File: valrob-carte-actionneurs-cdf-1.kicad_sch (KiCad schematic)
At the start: 99 parts, among them J1 USB_C_Receptacle_USB2.0_14P, J2 Conn_01x02, J3 Conn_01x02, J4 Conn_01x04_Pin, M1 Motor_Servo, M10 Motor_Servo, M11 Motor_Servo, M12 Motor_Servo, M13 Motor_Servo, M14 Motor_Servo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

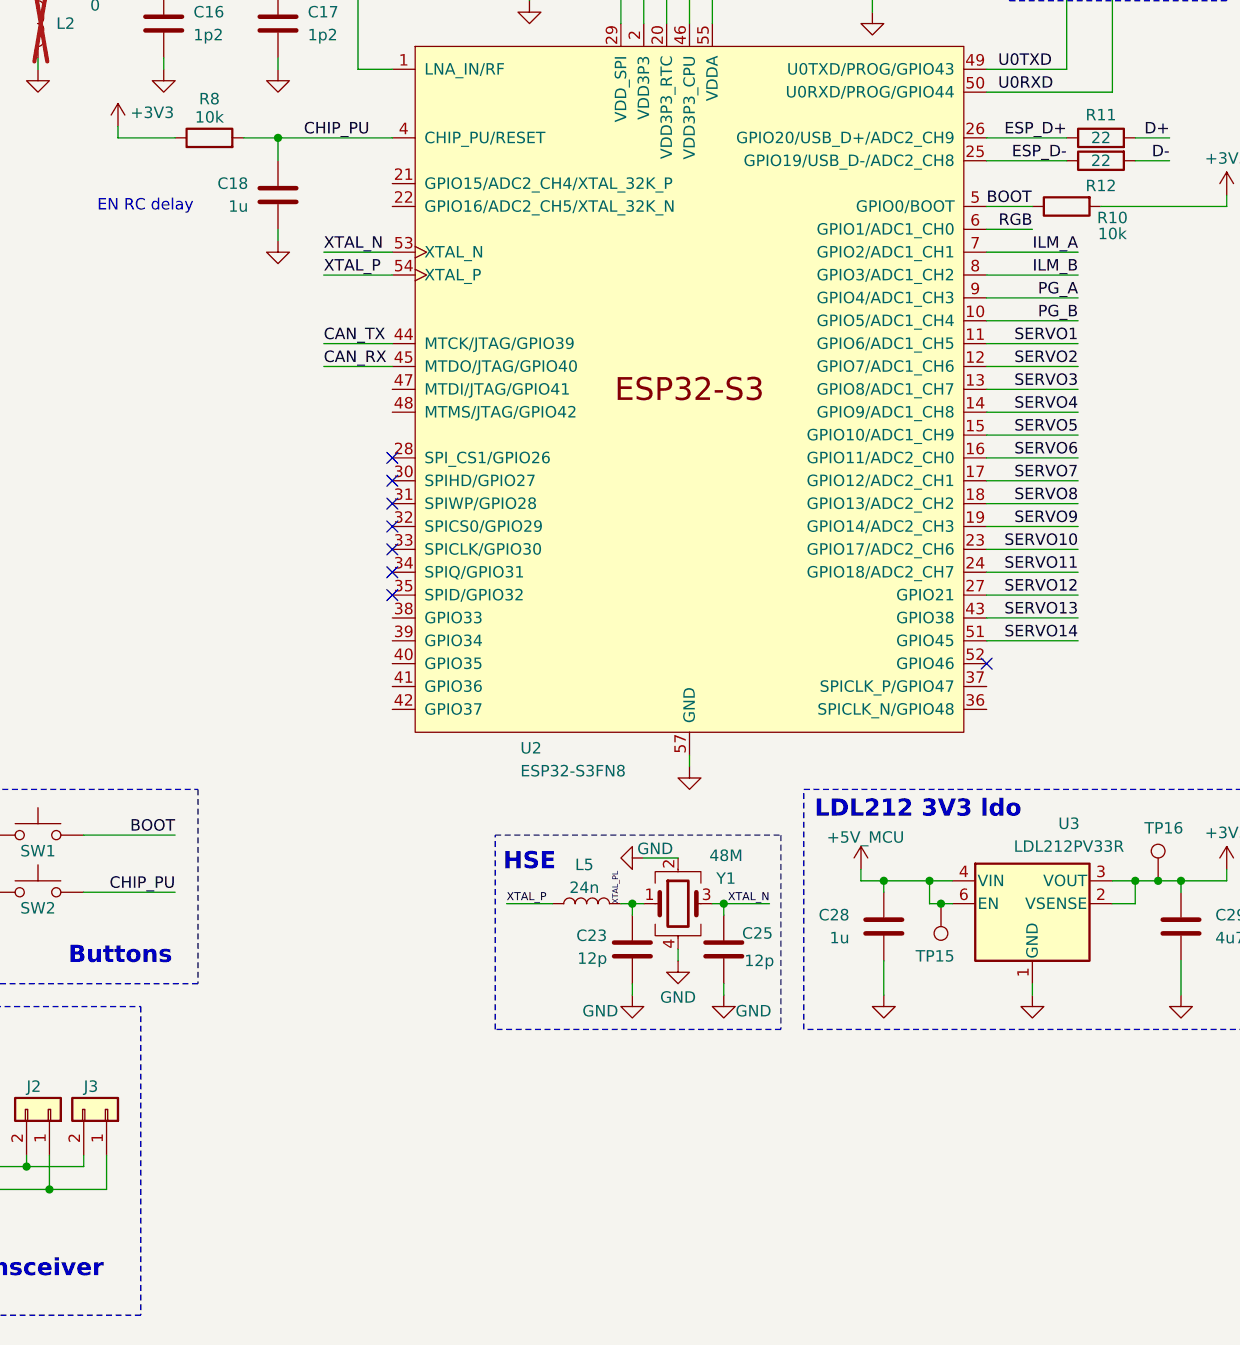
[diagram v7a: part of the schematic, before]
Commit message: schem: add extra GPIOs header
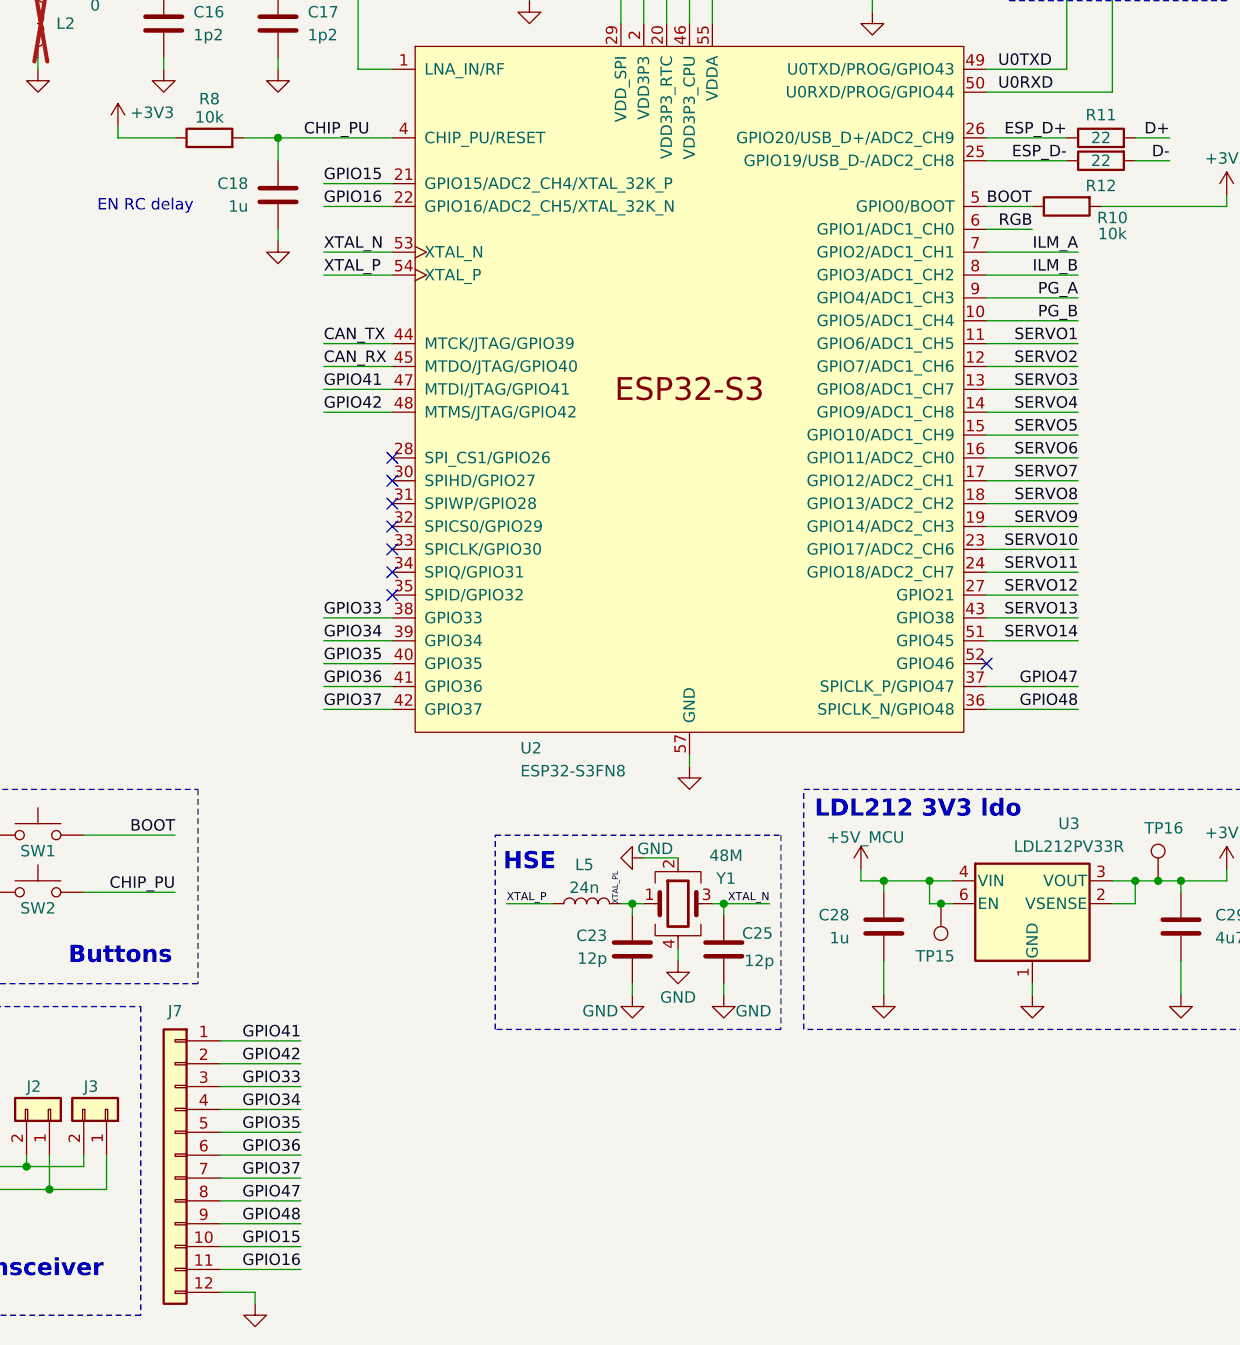
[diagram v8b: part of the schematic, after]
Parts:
- added J7: Conn_01x12, Connector_PinHeader_2.54mm:PinHeader_2x06_P2.54mm_Vertical, symbol Connector_Generic:Conn_01x12
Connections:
- net GND: now also J7.12 (Pin_12)
- net GPIO15: now reaches U2.21 (GPIO15/ADC2_CH4/XTAL_32K_P)
- net GPIO15: now also J7.10 (Pin_10)
- net GPIO16: now reaches U2.22 (GPIO16/ADC2_CH5/XTAL_32K_N)
- net GPIO16: now also J7.11 (Pin_11)
- net GPIO48: now reaches U2.36 (SPICLK_N/GPIO48)
- net GPIO48: now also J7.9 (Pin_9)
- net GPIO47: now reaches U2.37 (SPICLK_P/GPIO47)
- net GPIO47: now also J7.8 (Pin_8)
- net GPIO33: now reaches U2.38 (GPIO33)
- net GPIO33: now also J7.3 (Pin_3)
- net GPIO34: now reaches U2.39 (GPIO34)
- net GPIO34: now also J7.4 (Pin_4)
- net GPIO35: now reaches U2.40 (GPIO35)
- net GPIO35: now also J7.5 (Pin_5)
- net GPIO36: now reaches U2.41 (GPIO36)
- net GPIO36: now also J7.6 (Pin_6)
- net GPIO37: now reaches U2.42 (GPIO37)
- net GPIO37: now also J7.7 (Pin_7)
- net GPIO41: now reaches U2.47 (MTDI/JTAG/GPIO41)
- net GPIO41: now also J7.1 (Pin_1)
- net GPIO42: now reaches U2.48 (MTMS/JTAG/GPIO42)
- net GPIO42: now also J7.2 (Pin_2)
